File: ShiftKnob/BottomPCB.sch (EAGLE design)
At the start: 36 parts, among them IC2 UA78M05DCY, J1 AVR_SPI_PRG_6PTH, Q1 16MHz, Q2 MOSFET-NCHANNELSMD, Q3 MOSFET-PCHANNELSMD, Q4 MOSFET-NCHANNELSMD, Q5 MOSFET-NCHANNELSMD, Q6 MOSFET-NCHANNELSMD, U1 ATMEGA328, U3 FT232RL-BASICSSOP

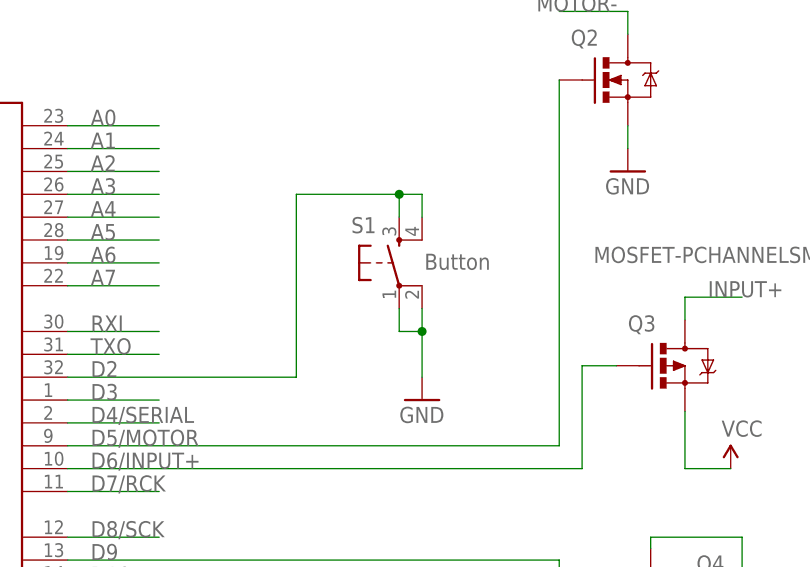
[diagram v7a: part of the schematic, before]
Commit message: add right angle button to schematic.
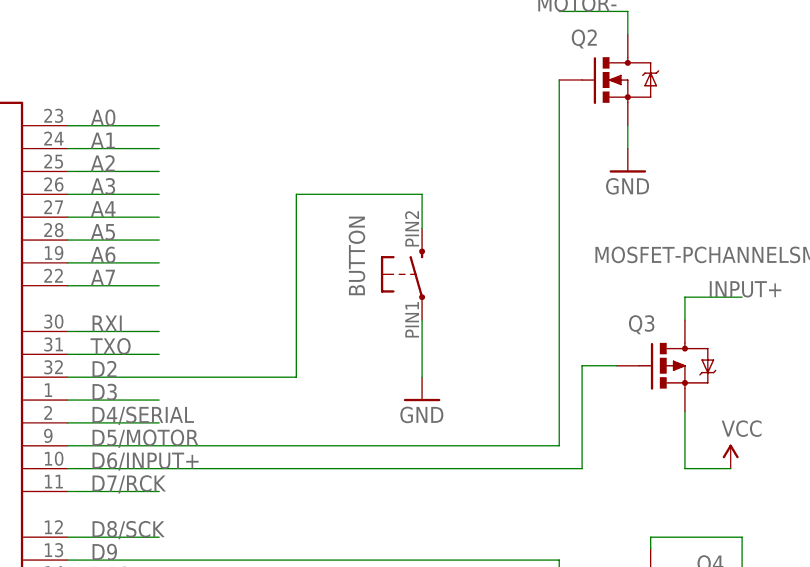
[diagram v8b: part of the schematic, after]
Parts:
- removed S1: Button, SparkFun:TAC_SWITCHSMD
- added BUTTON: BUTTON_RIGHTANGLE_SMD, FORD_frames:BUTTON_RIGHTANGLE_SMD
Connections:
- net D2: now also BUTTON.2; no longer S1.3, S1.4
- net GND: now also BUTTON.1; no longer S1.1, S1.2
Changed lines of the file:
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@@
 <part name="JP1" library="SparkFun-Connectors" deviceset="M06" device="SIP" value="6 PIN 90degree Header"/>
 <part name="R2" library="SparkFun" deviceset="RESISTOR" device="0402-RES" value="10K"/>
-<part name="S1" library="SparkFun" deviceset="TAC_SWITCH" device="SMD" value="Button"/>
 <part name="GND3" library="SparkFun" deviceset="GND" device=""/>
 <part name="C3" library="SparkFun" deviceset="CAP" device="0402-CAP" value="0.1uF"/>
@@
 <part name="P+4" library="SparkFun" deviceset="3.3V" device="" value="VCC"/>
 <part name="P+5" library="SparkFun" deviceset="3.3V" device="" value="VCC"/>
+<part name="BUTTON" library="FORD_frames" deviceset="BUTTON_RIGHTANGLE_SMD" device=""/>
 </parts>
 <sheets>
@@
 <instance part="JP1" gate="G$1" x="13.97" y="175.26"/>
 <instance part="R2" gate="G$1" x="27.94" y="135.89" rot="R90"/>
-<instance part="S1" gate="S" x="135.89" y="114.3" smashed="yes" rot="R90">
-<attribute name="NAME" x="130.556" y="117.602" size="1.778" layer="95"/>
-<attribute name="VALUE" x="138.684" y="113.538" size="1.778" layer="96"/>
-</instance>
 <instance part="GND3" gate="1" x="138.43" y="99.06"/>
 <instance part="C3" gate="G$1" x="33.02" y="57.15" smashed="yes" rot="R180">
@@
 <instance part="P+4" gate="G$1" x="232.41" y="115.57"/>
 <instance part="P+5" gate="G$1" x="260.35" y="115.57"/>
+<instance part="BUTTON" gate="G$1" x="138.43" y="113.03" smashed="yes" rot="R90">
+<attribute name="NAME" x="132.08" y="110.49" size="1.778" layer="95" rot="R90"/>
+</instance>
 </instances>
 <busses>
@@
 </segment>
 <segment>
-<wire x1="135.89" y1="109.22" x2="135.89" y2="106.68" width="0.1524" layer="91"/>
-<wire x1="135.89" y1="106.68" x2="138.43" y2="106.68" width="0.1524" layer="91"/>
-<wire x1="138.43" y1="106.68" x2="138.43" y2="109.22" width="0.1524" layer="91"/>
-<wire x1="138.43" y1="106.68" x2="138.43" y2="101.6" width="0.1524" layer="91"/>
-<junction x="138.43" y="106.68"/>
-<pinref part="S1" gate="S" pin="1"/>
-<pinref part="S1" gate="S" pin="2"/>
+<wire x1="138.43" y1="107.95" x2="138.43" y2="101.6" width="0.1524" layer="91"/>
 <pinref part="GND3" gate="1" pin="GND"/>
+<pinref part="BUTTON" gate="G$1" pin="1"/>
 </segment>
 <segment>
@@
 <segment>
 <label x="101.6" y="101.6" size="1.778" layer="95"/>
-<pinref part="S1" gate="S" pin="4"/>
-<wire x1="138.43" y1="121.92" x2="138.43" y2="119.38" width="0.1524" layer="91"/>
-<pinref part="S1" gate="S" pin="3"/>
-<wire x1="135.89" y1="121.92" x2="135.89" y2="119.38" width="0.1524" layer="91"/>
-<wire x1="135.89" y1="121.92" x2="138.43" y2="121.92" width="0.1524" layer="91"/>
+<wire x1="138.43" y1="121.92" x2="138.43" y2="118.11" width="0.1524" layer="91"/>
 <pinref part="U1" gate="G$1" pin="PD2(INT0)"/>
 <wire x1="99.06" y1="101.6" x2="124.46" y2="101.6" width="0.1524" layer="91"/>
 <wire x1="124.46" y1="101.6" x2="124.46" y2="121.92" width="0.1524" layer="91"/>
-<wire x1="124.46" y1="121.92" x2="135.89" y2="121.92" width="0.1524" layer="91"/>
-<junction x="135.89" y="121.92"/>
-</segment>
-</net>
+<wire x1="124.46" y1="121.92" x2="138.43" y2="121.92" width="0.1524" layer="91"/>
+<pinref part="BUTTON" gate="G$1" pin="2"/>
+</segment>
+</net>
